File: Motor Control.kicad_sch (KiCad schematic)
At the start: 46 parts, among them J1 Conn_01x05_Pin, J2 Conn_01x06_Pin, J3 USB_B, J5 Conn_01x02_Socket, J6 Conn_01x02_Socket, SW1 RotaryEncoder_Switch_MP, U10 LM317_TO-220, U3 PIC18F26K22-xSP, U4 MCP2221AxP, U5 L78L05_TO92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

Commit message: Placement H bridge & PSU
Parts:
- removed C11, C4, C8: 100nF, Capacitor_THT:C_Rect_L7.2mm_W2.5mm_P5.00mm_FKS2_FKP2_MKS2_MKP2, symbol Device:C
- removed C12: 150pF, Capacitor_THT:C_Rect_L7.2mm_W2.5mm_P5.00mm_FKS2_FKP2_MKS2_MKP2, symbol Device:C
- removed C14: 330uF, Capacitor_THT:CP_Radial_D8.0mm_P5.00mm, symbol Device:C_Polarized
- removed C15, C16: 1uF, Capacitor_THT:CP_Radial_D5.0mm_P2.50mm, symbol Device:C_Polarized
- removed C9: 10nF, Capacitor_THT:C_Rect_L7.2mm_W2.5mm_P5.00mm_FKS2_FKP2_MKS2_MKP2, symbol Device:C
- removed D3, D4: 1N4148, Diode_THT:D_DO-35_SOD27_P7.62mm_Horizontal, symbol Diode:1N4148
- removed F1: Fuse, User:Fuseholder_Stelvio-kontek_PTF_78_5x20mm, symbol Device:Fuse
- removed J5: Conn_01x02_Socket, Connector_Phoenix_MC_HighVoltage:PhoenixContact_MCV_1,5_2-G-5.08_1x02_P5.08mm_Vertical, symbol Connector:Conn_01x02_Socket
- removed R33: 68R, Resistor_THT:R_Axial_DIN0207_L6.3mm_D2.5mm_P10.16mm_Horizontal, symbol Device:R
- removed R44: 3k3, Resistor_THT:R_Axial_DIN0207_L6.3mm_D2.5mm_P10.16mm_Horizontal, symbol Device:R
- removed R45: 390, Resistor_THT:R_Axial_DIN0207_L6.3mm_D2.5mm_P10.16mm_Horizontal, symbol Device:R
- removed U10: LM317_TO-220, Package_TO_SOT_THT:TO-220-3_Horizontal_TabDown, symbol Regulator_Linear:LM317_TO-220
- removed U5: L78L05_TO92, Package_TO_SOT_THT:TO-92_Inline_Wide, symbol Regulator_Linear:L78L05_TO92
- removed U8: HCPL7510, Package_DIP:DIP-8_W7.62mm_Socket_LongPads, symbol User:HCPL-7510
- U3: footprint Package_DIP:DIP-28_W7.62mm -> Package_DIP:DIP-28_W7.62mm_Socket_LongPads
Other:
- added sheet PSU (PSU.kicad_sch)
- sheet H Bridge ports: added GNDPWR_{out}, P1A, P1B, P1C, P1D; removed none

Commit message: Update 090725
New footprints added
Schematic made into sub schematics
PCB needs work
Component references need to be sorted for the most part
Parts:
- removed C1, C10, C13, C5, C7: 100nF, Capacitor_THT:C_Rect_L7.2mm_W2.5mm_P5.00mm_FKS2_FKP2_MKS2_MKP2, symbol Device:C
- removed C3: 470nF, Capacitor_THT:C_Rect_L7.2mm_W2.5mm_P5.00mm_FKS2_FKP2_MKS2_MKP2, symbol Device:C_Small
- removed DS1: WC1602A, Display:WC1602A, symbol Display_Character:WC1602A
- removed J1: Conn_01x05_Pin, Connector_PinSocket_2.54mm:PinSocket_1x05_P2.54mm_Horizontal, symbol Connector:Conn_01x05_Pin
- removed J2: Conn_01x06_Pin, Connector_PinHeader_2.54mm:PinHeader_1x06_P2.54mm_Vertical, symbol Connector:Conn_01x06_Pin
- removed J3: USB_B, Connector_USB:USB_B_TE_5787834_Vertical, symbol Connector:USB_B
- removed J6: Conn_01x02_Socket, Connector_Phoenix_MC_HighVoltage:PhoenixContact_MCV_1,5_2-G-5.08_1x02_P5.08mm_Vertical, symbol Connector:Conn_01x02_Socket
- removed L1: L_Ferrite_Small, symbol Device:L_Ferrite_Small
- removed R19, R29, R32, R39, R4, R5: 10k, Resistor_THT:R_Axial_DIN0207_L6.3mm_D2.5mm_P10.16mm_Horizontal, symbol Device:R
- removed R23, R27, R41, R42: 1k, Resistor_THT:R_Axial_DIN0207_L6.3mm_D2.5mm_P10.16mm_Horizontal, symbol Device:R_Small
- removed R43: 10k, Resistor_THT:R_Axial_DIN0207_L6.3mm_D2.5mm_P10.16mm_Horizontal, symbol Device:R_Small
- removed RV1: 50k, Potentiometer_THT:Potentiometer_Piher_PT-10-V05_Vertical, symbol Device:R_Potentiometer
- removed SW1: RotaryEncoder_Switch_MP, Rotary_Encoder:RotaryEncoder_Alps_EC11E-Switch_Vertical_H20mm, symbol Device:RotaryEncoder_Switch_MP
- removed U3: PIC18F26K22-xSP, Package_DIP:DIP-28_W7.62mm_Socket_LongPads, symbol MCU_Microchip_PIC18:PIC18F26K22-xSP
- removed U4: MCP2221AxP, Package_DIP:DIP-14_W7.62mm_Socket_LongPads, symbol Interface_USB:MCP2221AxP
- removed U9: 74AHC595, Package_DIP:DIP-16_W7.62mm_Socket_LongPads, symbol 74xx:74AHC595
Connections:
- no-connect marks 12 -> 0
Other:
- added sheet Disp & encoder (dispEncoder.kicad_sch)
- added sheet MCU & USB (MCU_USB.kicad_sch)

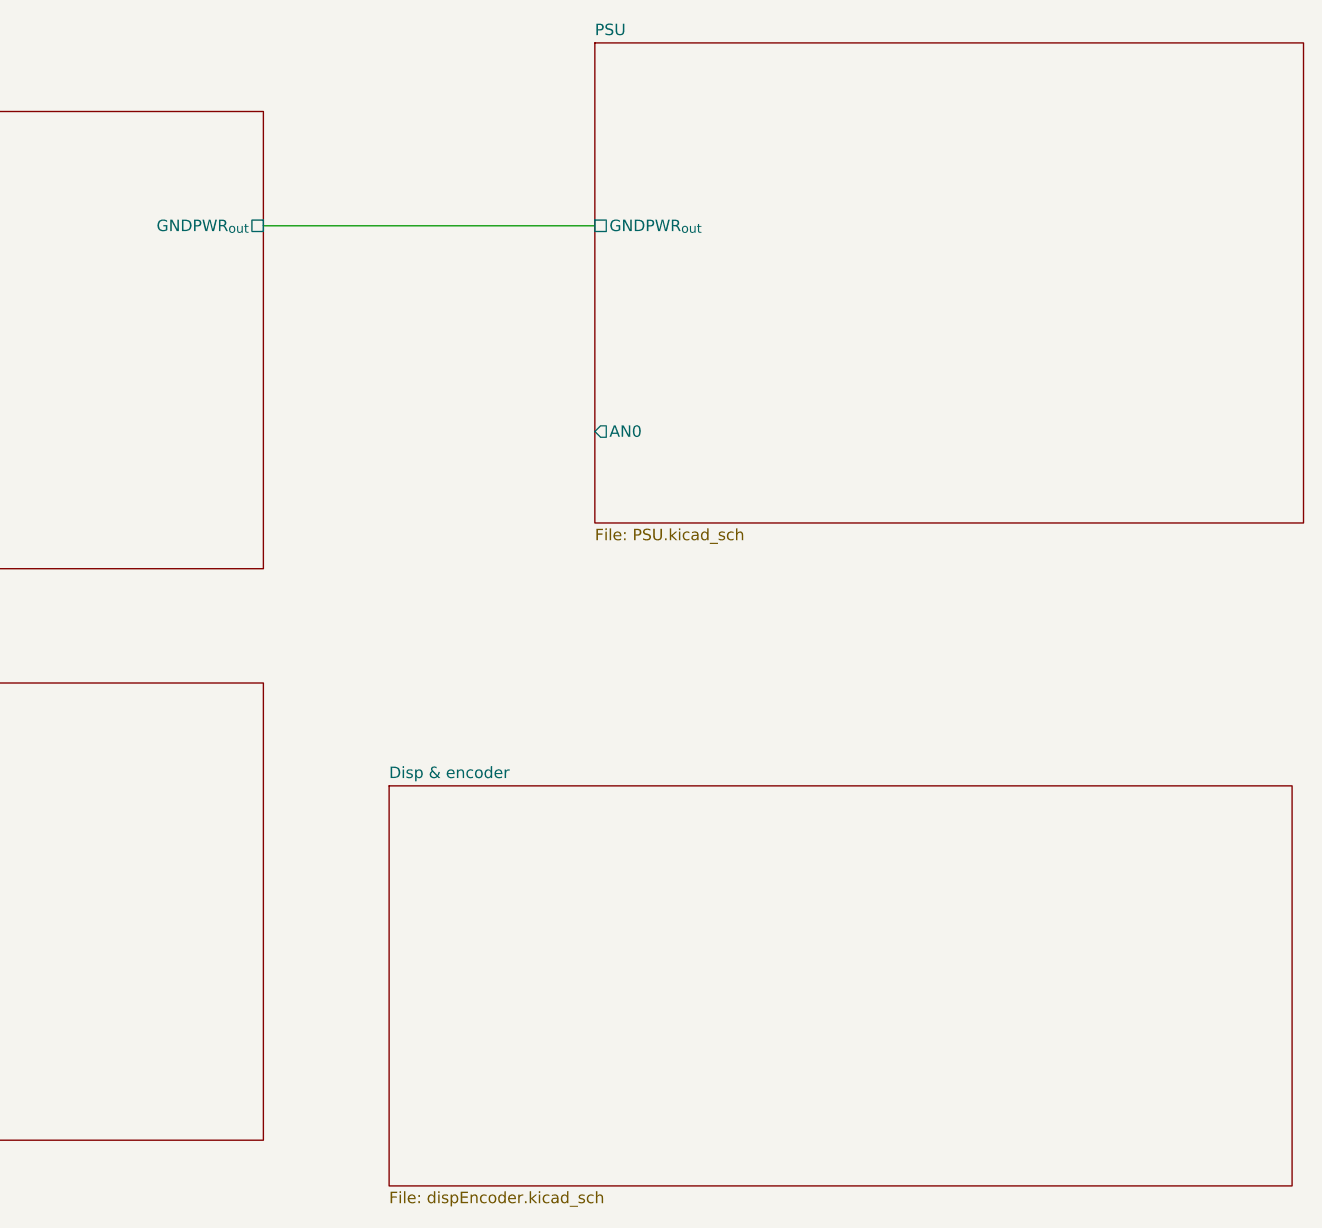
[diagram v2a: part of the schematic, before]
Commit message: Almost done
Schematic done
PCB missing ground planes
Need Coopilot review
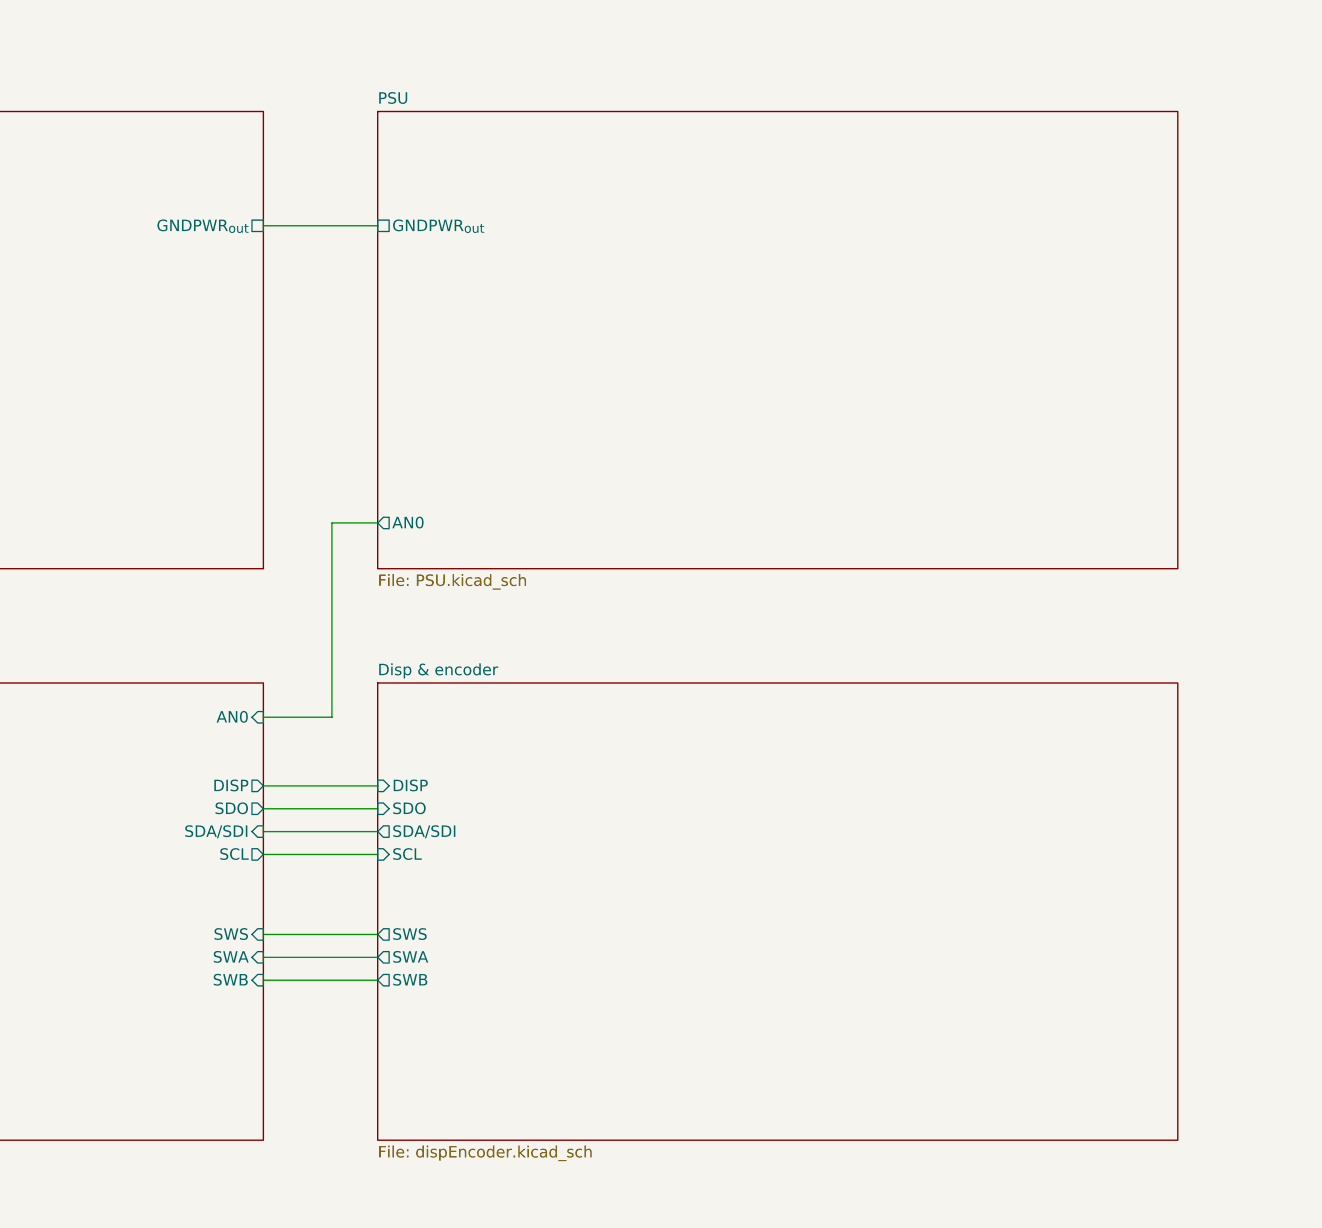
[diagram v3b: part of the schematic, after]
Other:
- sheet Disp & encoder ports: added DISP, SCL, SDA/SDI, SDO, SWA, SWB, SWS; removed none
- sheet MCU & USB ports: added AN0, DISP, SCL, SDA/SDI, SDO, SWA, SWB, SWS; removed none

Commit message: V 2.0
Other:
- sheet Disp & encoder ports: added DISP_{SS}, MOSI/PGD, SCL/PGC; removed DISP, SDA/SDI, SDO
- sheet MCU & USB ports: added AN, DISP_{SS}, MOSI_1, MOSI_{1}/PGD, SCL_1, SCL_{1}/PGC; removed AN0, DISP, SCL, SDA/SDI, SDO
- sheet PSU ports: added AN; removed AN0
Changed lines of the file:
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@@
+	(wire
+		(pts
+			(xy 114.3 118.11) (xy 127 118.11)
+		)
+		(stroke
+			(width 0)
+			(type default)
+		)
+	)
 	(wire
 		(pts
@@
 		(pts
 			(xy 114.3 129.54) (xy 127 129.54)
-		)
-		(stroke
-			(width 0)
-			(type default)
-		)
-	)
-	(wire
-		(pts
-			(xy 114.3 118.11) (xy 127 118.11)
 		)
 		(stroke
@@
 			)
 		)
-		(pin "AN0" input
+		(pin "AN" input
 			(at 114.3 105.41 0)
-			(effects
-				(font
-					(size 1.27 1.27)
-				)
-				(justify right)
-			)
-		)
-		(pin "SCL" output
-			(at 114.3 120.65 0)
-			(effects
-				(font
-					(size 1.27 1.27)
-				)
-				(justify right)
-			)
-		)
-		(pin "SDA{slash}SDI" input
-			(at 114.3 118.11 0)
-			(effects
-				(font
-					(size 1.27 1.27)
-				)
-				(justify right)
-			)
-		)
-		(pin "SDO" output
-			(at 114.3 115.57 0)
 			(effects
 				(font
@@
 			)
 		)
-		(pin "DISP" output
+		(pin "DISP_{SS}" output
 			(at 114.3 113.03 0)
+			(effects
+				(font
+					(size 1.27 1.27)
+				)
+				(justify right)
+			)
+		)
+		(pin "MOSI_1" output
+			(at 25.4 115.57 180)
+			(effects
+				(font
+					(size 1.27 1.27)
+				)
+				(justify left)
+			)
+		)
+		(pin "SCL_1" output
+			(at 114.3 120.65 0)
+			(effects
+				(font
+					(size 1.27 1.27)
+				)
+				(justify right)
+			)
+		)
+		(pin "MOSI_{1}{slash}PGD" output
+			(at 114.3 115.57 0)
+			(effects
+				(font
+					(size 1.27 1.27)
+				)
+				(justify right)
+			)
+		)
+		(pin "SCL_{1}{slash}PGC" output
+			(at 114.3 118.11 0)
 			(effects
 				(font
@@
 			)
 		)
-		(pin "DISP" input
-			(at 127 113.03 180)
-			(effects
-				(font
-					(size 1.27 1.27)
-				)
-				(justify left)
-			)
-		)
 		(pin "SCL" input
 			(at 127 120.65 180)
@@
 			)
 		)
-		(pin "SDA{slash}SDI" output
-			(at 127 118.11 180)
-			(effects
-				(font
-					(size 1.27 1.27)
-				)
-				(justify left)
-			)
-		)
-		(pin "SDO" input
-			(at 127 115.57 180)
-			(effects
-				(font
-					(size 1.27 1.27)
-				)
-				(justify left)
-			)
-		)
 		(pin "SWA" output
 			(at 127 132.08 180)
@@
 		(pin "SWS" output
 			(at 127 129.54 180)
+			(effects
+				(font
+					(size 1.27 1.27)
+				)
+				(justify left)
+			)
+		)
+		(pin "DISP_{SS}" input
+			(at 127 113.03 180)
+			(effects
+				(font
+					(size 1.27 1.27)
+				)
+				(justify left)
+			)
+		)
+		(pin "MOSI{slash}PGD" input
+			(at 127 115.57 180)
+			(effects
+				(font
+					(size 1.27 1.27)
+				)
+				(justify left)
+			)
+		)
+		(pin "SCL{slash}PGC" input
+			(at 127 118.11 180)
 			(effects
 				(font
@@
 			)
 		)
-		(pin "AN0" output
+		(pin "AN" output
 			(at 127 83.82 180)
 			(effects
